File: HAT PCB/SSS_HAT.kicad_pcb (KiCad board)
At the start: 2 copper layers, 24 parts, among them J1 Conn_01x22_Socket, J2 Conn_01x22_Socket, J3 CAN0, J4 CAN1, J5 I2C0, J6 I2C1, SW1 CAN0_Pulldown, SW2 CAN1_Pulldown, SW3 I2C0_Pulldown, SW4 I2C1_Pulldown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

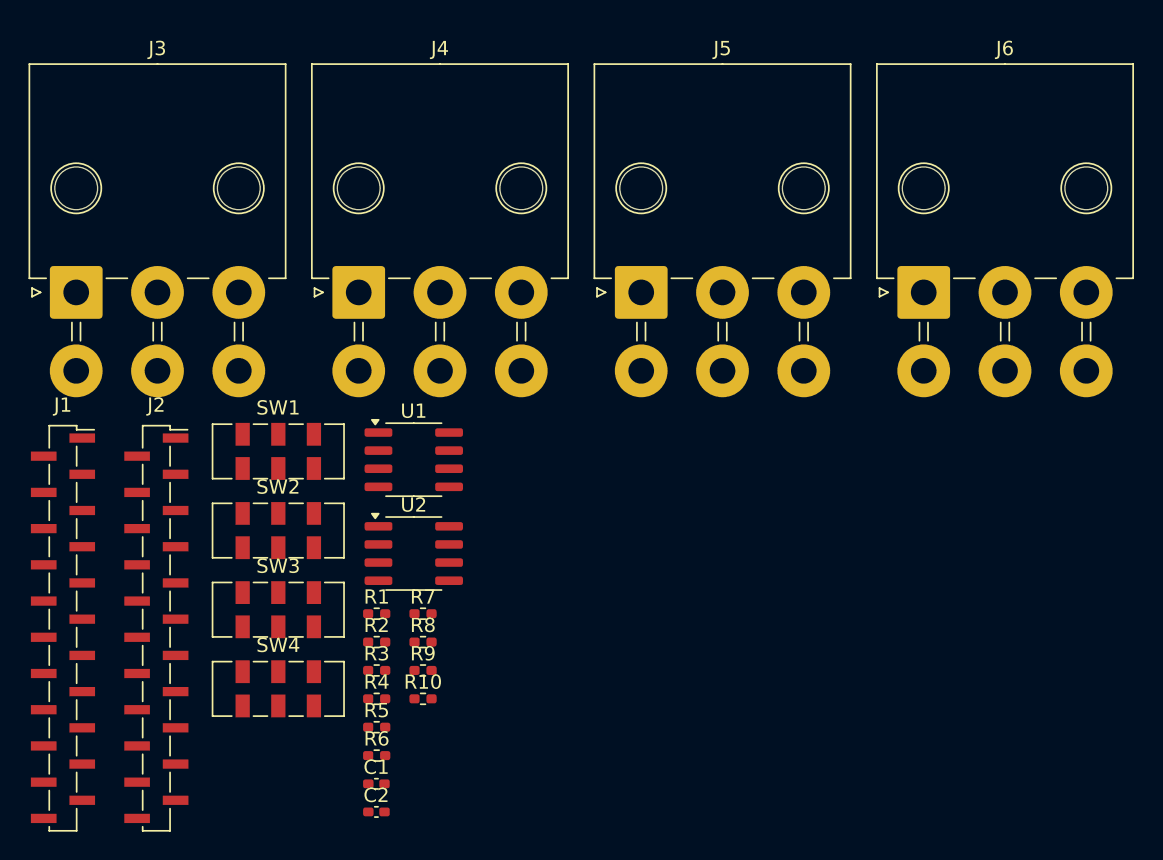
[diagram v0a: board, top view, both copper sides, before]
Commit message: Added 2 Channel 18-bit ADC
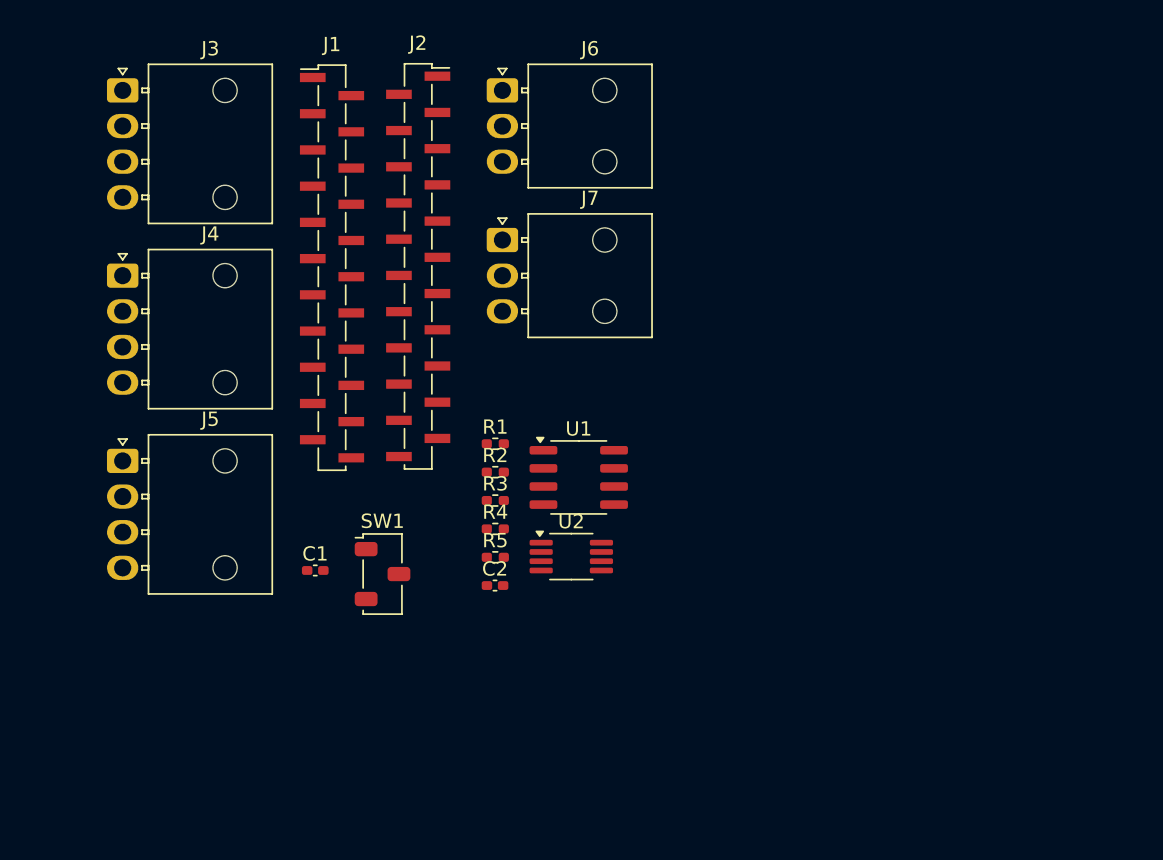
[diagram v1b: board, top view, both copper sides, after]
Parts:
- removed R10, R7, R8, R9: 2k2, Resistor_SMD:R_0402_1005Metric_Pad0.72x0.64mm_HandSolder
- removed R6: 60, Resistor_SMD:R_0402_1005Metric_Pad0.72x0.64mm_HandSolder
- removed SW2: CAN1_Pulldown, Button_Switch_SMD:SW_DPDT_CK_JS202011JCQN
- removed SW3: I2C0_Pulldown, Button_Switch_SMD:SW_DPDT_CK_JS202011JCQN
- removed SW4: I2C1_Pulldown, Button_Switch_SMD:SW_DPDT_CK_JS202011JCQN
- added J7: ADC_1, Connector_Molex:Molex_Nano-Fit_105313-xx03_1x03_P2.50mm_Horizontal, F.Cu at (152.1, 58.3)
- C1: value 4.7nF -> 0.1μF
- C2: value 4.7nF -> 10μF
- J1: value Conn_01x22_Socket -> ESP32_Connector_0; footprint Connector_PinSocket_1.27mm:PinSocket_1x22_P1.27mm_Vertical_SMD_Pin1Right -> Connector_PinSocket_1.27mm:PinSocket_1x22_P1.27mm_Vertical_SMD_Pin1Left
- J2: value Conn_01x22_Socket -> ESP32_Connector_1
- J3: value CAN0 -> CAN; footprint Connector_Molex:Molex_Mega-Fit_76825-0006_2x03_P5.70mm_Horizontal -> Connector_Molex:Molex_Nano-Fit_105313-xx04_1x04_P2.50mm_Horizontal
- J4: value CAN1 -> CAN; footprint Connector_Molex:Molex_Mega-Fit_76825-0006_2x03_P5.70mm_Horizontal -> Connector_Molex:Molex_Nano-Fit_105313-xx04_1x04_P2.50mm_Horizontal
- J5: value I2C0 -> I2C; footprint Connector_Molex:Molex_Mega-Fit_76825-0006_2x03_P5.70mm_Horizontal -> Connector_Molex:Molex_Nano-Fit_105313-xx04_1x04_P2.50mm_Horizontal
- J6: value I2C1 -> ADC_0; footprint Connector_Molex:Molex_Mega-Fit_76825-0006_2x03_P5.70mm_Horizontal -> Connector_Molex:Molex_Nano-Fit_105313-xx03_1x03_P2.50mm_Horizontal
- R2, R3, R5: value 60 -> 2k2
- R4: value 120 -> 2k2
- SW1: value CAN0_Pulldown -> I2C; footprint Button_Switch_SMD:SW_DPDT_CK_JS202011JCQN -> Button_Switch_SMD:Nidec_Copal_CAS-120A
- U2: value TJA1051T -> MCP3422Axx-xMS; footprint Package_SO:SOIC-8_3.9x4.9mm_P1.27mm -> Package_SO:MSOP-8_3x3mm_P0.65mm
- moved J5 38.2 mm to (125.4, 73.8)
- moved J6 32.8 mm to (152.1, 47.8)
- moved J1 31.5 mm to (140.1, 60.3)
- moved J2 31.3 mm to (146.2, 60.2)
- moved C2 17.9 mm to (151.5, 82.6)
- moved J4 16.6 mm to (125.4, 60.8)
- moved C1 15.6 mm to (138.9, 81.5)
- moved J3 14.5 mm to (125.4, 47.8)
- moved R1 14.5 mm to (151.6, 72.6)
- moved R3 14.5 mm to (151.6, 76.6)
- moved R4 14.5 mm to (151.6, 78.6)
- moved R2 14.5 mm to (151.6, 74.6)
- moved R5 14.5 mm to (151.6, 80.6)
- moved U1 11.6 mm to (157.4, 75.0)
- moved SW1 11.3 mm to (143.7, 81.8)
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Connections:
- net CAN0_RX renamed CAN_RX
- net CAN0_TX renamed CAN_TX
- C1 pad 1: Net-(C1-Pad1) -> +3.3V
- C2 pad 1: Net-(C2-Pad1) -> +3.3V
- J1 pad 12: ADC1_7 -> unconnected-(J1-Pin_12-Pad12)
- J1 pad 13: ADC1_2 -> unconnected-(J1-Pin_13-Pad13)
- J1 pad 19: CAN0_S -> unconnected-(J1-Pin_19-Pad19)
- J1 pad 20: CAN1_S -> unconnected-(J1-Pin_20-Pad20)
- J1 pad 6: ADC1_5 -> unconnected-(J1-Pin_6-Pad6)
- J1 pad 7: ADC1_6 -> unconnected-(J1-Pin_7-Pad7)
- J1 pad 8: CAN1_TX -> CAN_S
- J1 pad 9: CAN1_RX -> unconnected-(J1-Pin_9-Pad9)
- J2 pad 4: ADC1_0 -> unconnected-(J2-Pin_4-Pad4)
- J2 pad 5: ADC1_1 -> unconnected-(J2-Pin_5-Pad5)
- J2 pad 6: I2C0_SDA -> I2C_SDA
- J2 pad 7: I2C0_SCL -> I2C_SCL
- J2 pad 8: I2C1_SDA -> ADC_SDA
- J2 pad 9: I2C1_SCL -> ADC_SCL
- J3 pad 1: Net-(J3-Pin_1) -> +5V
- J3 pad 2: unconnected-(J3-Pin_2-Pad2) -> GND
- J3 pad 3: Net-(J3-Pin_3) -> CANH
- J3 pad 4: +5V -> CANL
- J4 pad 1: Net-(J4-Pin_1) -> +5V
- J4 pad 2: unconnected-(J4-Pin_2-Pad2) -> GND
- J4 pad 3: Net-(J4-Pin_3) -> CANH
- J4 pad 4: +5V -> CANL
- J5 pad 1: I2C0_SCL -> +5V
- J5 pad 2: unconnected-(J5-Pin_2-Pad2) -> GND
- J5 pad 3: I2C0_SDA -> I2C_SCL
- J5 pad 4: +5V -> I2C_SDA
- J6 pad 1: I2C1_SCL -> +5V
- J6 pad 2: unconnected-(J6-Pin_2-Pad2) -> GND
- J6 pad 3: I2C1_SDA -> ADC_0
- R1 pad 1: Net-(J3-Pin_3) -> CANL
- R1 pad 2: Net-(J3-Pin_1) -> CANH
- R2 pad 1: Net-(SW1A-A) -> Net-(SW1-C)
- R2 pad 2: Net-(C1-Pad1) -> I2C_SCL
- R3 pad 1: Net-(SW1B-A) -> Net-(SW1-C)
- R3 pad 2: Net-(C1-Pad1) -> I2C_SDA
- R4 pad 1: Net-(J4-Pin_3) -> +3.3V
- R4 pad 2: Net-(J4-Pin_1) -> ADC_SCL
- R5 pad 1: Net-(SW2A-A) -> +3.3V
- R5 pad 2: Net-(C2-Pad1) -> ADC_SDA
- SW1 pad 1: Net-(SW1A-A) -> Net-(SW1-C)
- SW1 pad 2: Net-(J3-Pin_1) -> +3.3V
- U1 pad 6: Net-(J3-Pin_3) -> CANL
- U1 pad 7: Net-(J3-Pin_1) -> CANH
- U1 pad 8: CAN0_S -> CAN_S
- U2 pad 1: CAN1_TX -> ADC_0
- U2 pad 3: +5V -> +3.3V
- U2 pad 4: CAN1_RX -> ADC_SDA
- U2 pad 5: unconnected-(U2-NC-Pad5) -> ADC_SCL
- U2 pad 6: Net-(J4-Pin_3) -> GND
- U2 pad 7: Net-(J4-Pin_1) -> ADC_2
- U2 pad 8: CAN1_S -> GND
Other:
- copper layers 2 -> 4

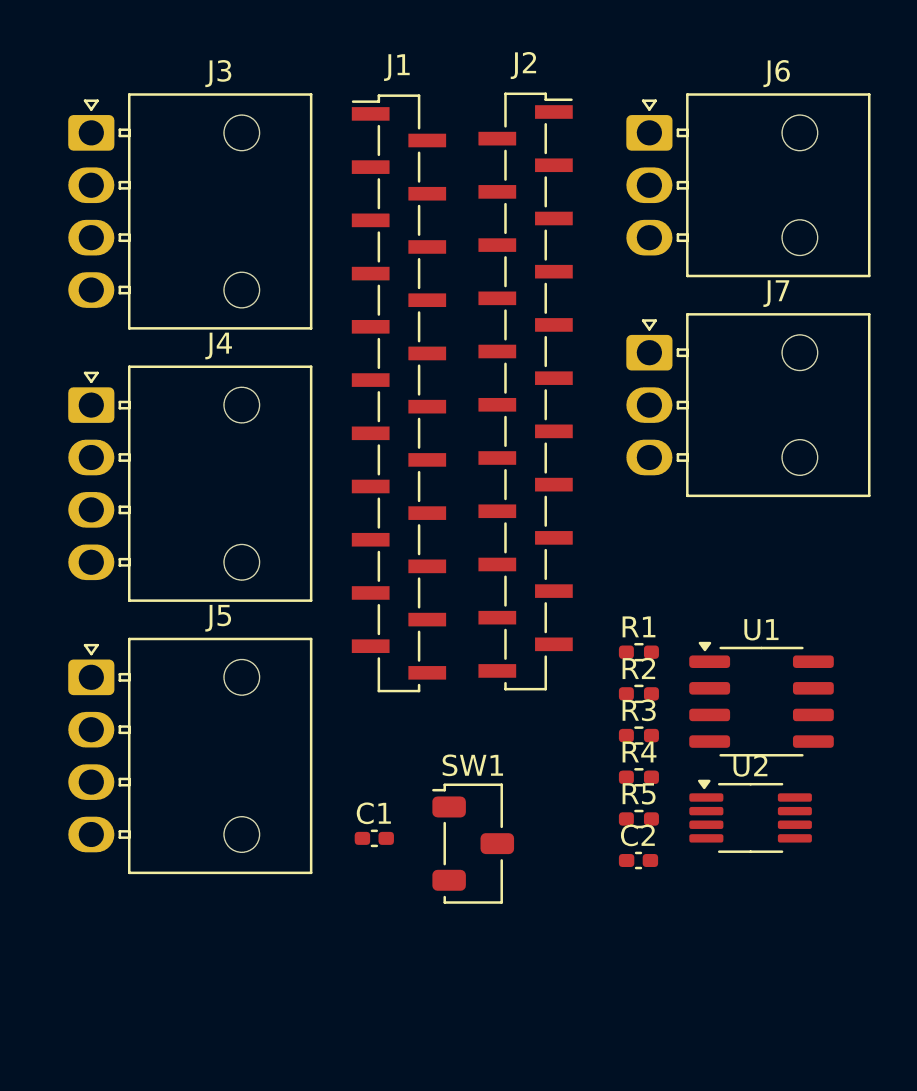
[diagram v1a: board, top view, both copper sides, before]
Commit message: added IMU
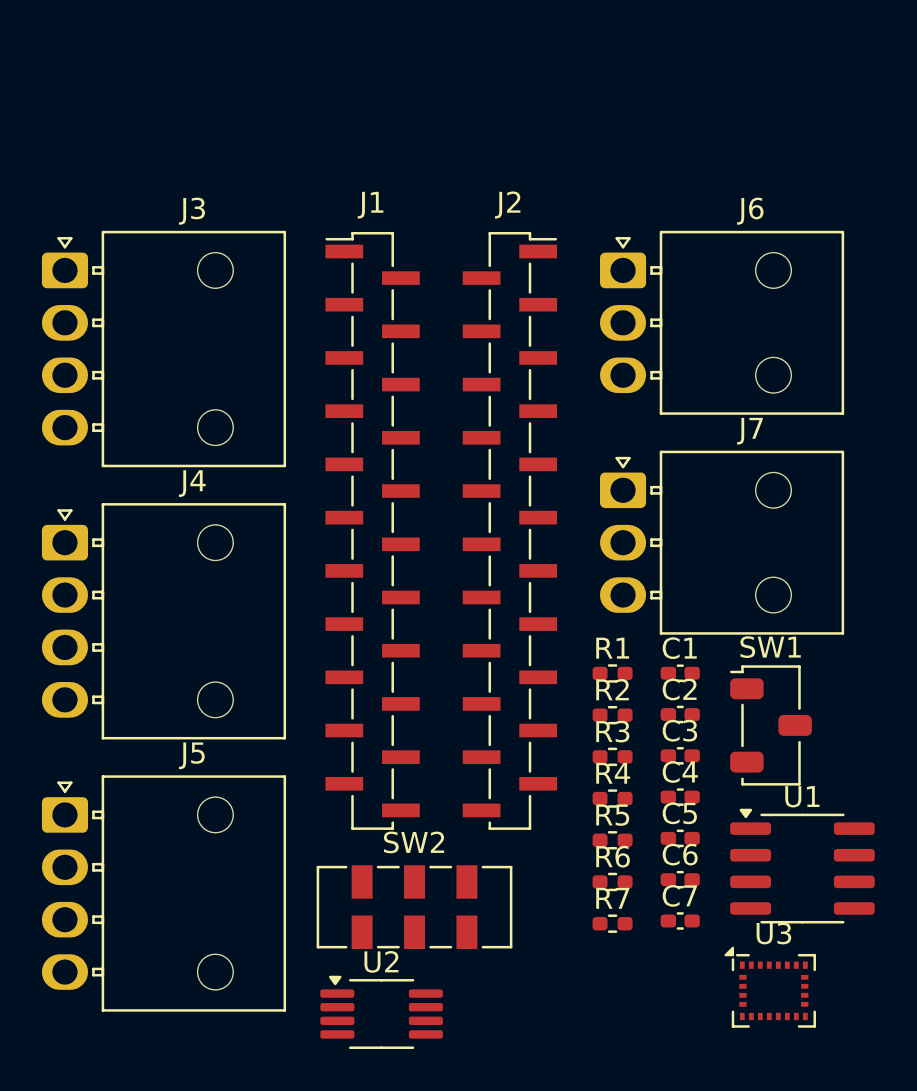
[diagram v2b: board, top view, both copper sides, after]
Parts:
- added C3: 0.1μF, Capacitor_SMD:C_0402_1005Metric_Pad0.74x0.62mm_HandSolder, F.Cu at (153.5, 77.6)
- added C4: 10μF, Capacitor_SMD:C_0402_1005Metric_Pad0.74x0.62mm_HandSolder, F.Cu at (153.5, 79.5)
- added C5: 0.1μF, Capacitor_SMD:C_0402_1005Metric_Pad0.74x0.62mm_HandSolder, F.Cu at (153.5, 81.5)
- added C6: 10nF, Capacitor_SMD:C_0402_1005Metric_Pad0.74x0.62mm_HandSolder, F.Cu at (153.5, 83.5)
- added C7: 0.1μF, Capacitor_SMD:C_0402_1005Metric_Pad0.74x0.62mm_HandSolder, F.Cu at (153.5, 85.4)
- added R6: 10k, Resistor_SMD:R_0402_1005Metric_Pad0.72x0.64mm_HandSolder, F.Cu at (150.3, 83.6)
- added R7: 10k, Resistor_SMD:R_0402_1005Metric_Pad0.72x0.64mm_HandSolder, F.Cu at (150.3, 85.6)
- added SW2: IMU_SPI_Pullup, Button_Switch_SMD:SW_DPDT_CK_JS202011JCQN, F.Cu at (140.8, 84.8)
- added U3: LSM9DS1, Package_LGA:LGA-24L_3x3.5mm_P0.43mm, F.Cu at (158.0, 88.8)
- R2, R3: value 2k2 -> 10k
- moved U2 19.9 mm to (139.3, 89.9)
- moved C1 16.6 mm to (153.5, 73.6)
- moved SW1 15.3 mm to (157.9, 76.1)
- moved U1 8.20 mm to (159.4, 82.9)
- moved C2 7.24 mm to (153.5, 75.6)
- moved J2 6.70 mm to (145.4, 66.8)
- moved J1 6.68 mm to (138.8, 66.8)
- moved J3 6.68 mm to (124.2, 54.4)
- moved J4 6.68 mm to (124.2, 67.4)
- moved J5 6.68 mm to (124.2, 80.4)
- moved J6 6.68 mm to (150.8, 54.4)
- moved J7 6.68 mm to (150.8, 64.9)
- moved R1 1.62 mm to (150.3, 73.6)
- moved R2 1.62 mm to (150.3, 75.6)
- moved R3 1.62 mm to (150.3, 77.6)
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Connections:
- J1 pad 10: unconnected-(J1-Pin_10-Pad10) -> IMU_SDA
- J1 pad 11: unconnected-(J1-Pin_11-Pad11) -> IMU_SCL

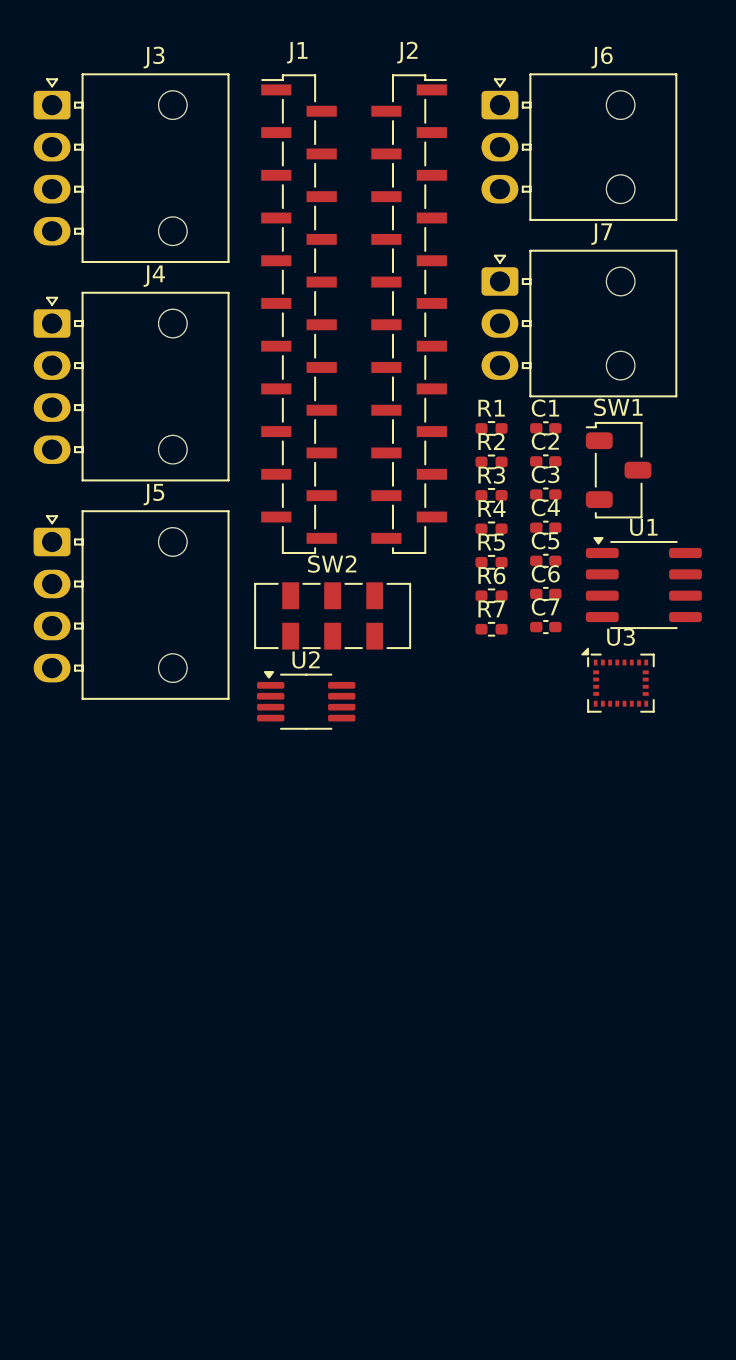
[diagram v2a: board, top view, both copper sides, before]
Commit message: Routed PCB & Replaced IMU for ICM-42688-P
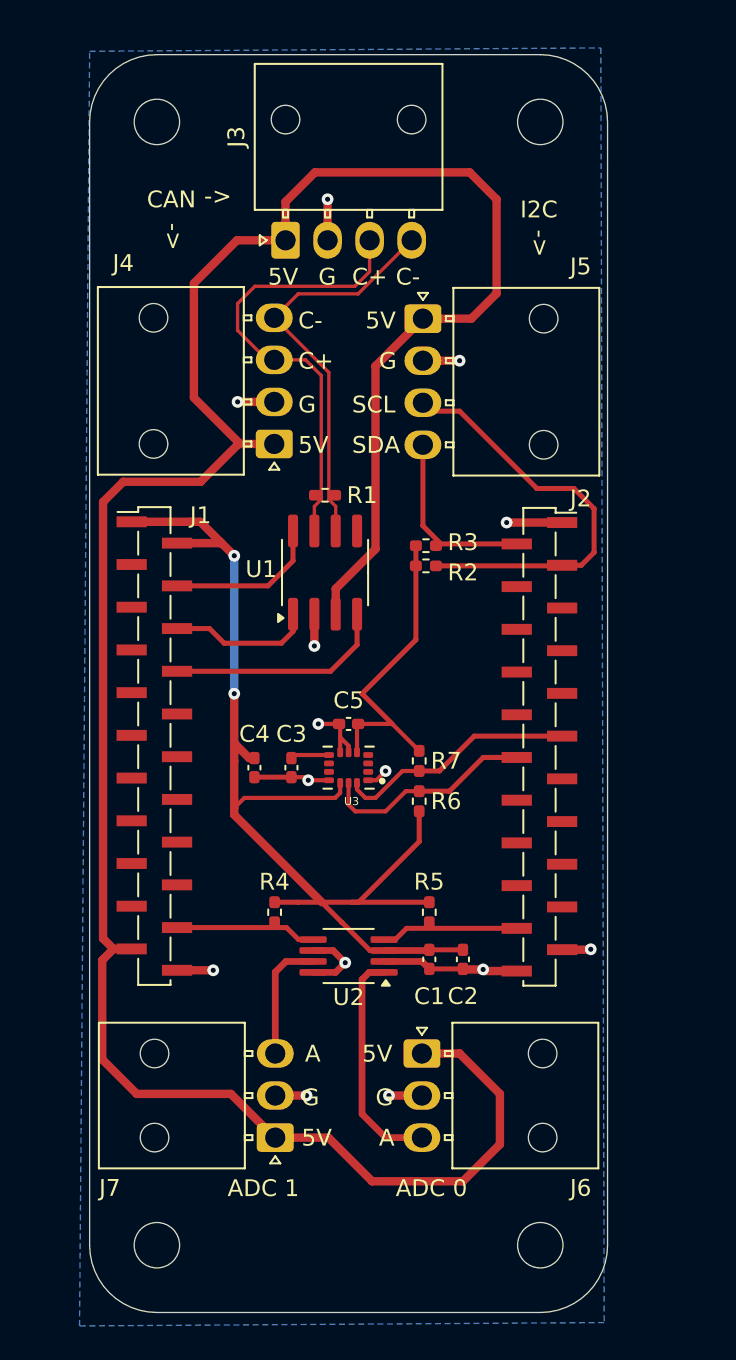
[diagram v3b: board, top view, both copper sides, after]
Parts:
- removed C6: 10nF, Capacitor_SMD:C_0402_1005Metric_Pad0.74x0.62mm_HandSolder
- removed C7: 0.1μF, Capacitor_SMD:C_0402_1005Metric_Pad0.74x0.62mm_HandSolder
- removed SW1: I2C, Button_Switch_SMD:Nidec_Copal_CAS-120A
- removed SW2: IMU_SPI_Pullup, Button_Switch_SMD:SW_DPDT_CK_JS202011JCQN
- added H1: MountingHole, MountingHole:MountingHole_2.7mm_M2.5, F.Cu at (130.4, 55.4)
- added H2: MountingHole, MountingHole:MountingHole_2.7mm_M2.5, F.Cu at (153.2, 55.4)
- added H3: MountingHole, MountingHole:MountingHole_2.7mm_M2.5, F.Cu at (153.2, 122.2)
- added H4: MountingHole, MountingHole:MountingHole_2.7mm_M2.5, F.Cu at (130.4, 122.2)
- C4: value 10μF -> 2.2μF
- U3: value LSM9DS1 -> ICM-42688-P; footprint Package_LGA:LGA-24L_3x3.5mm_P0.43mm -> ICM-42688-P:PQFN50P300X250X97-14N
- moved J6 56.6 mm to (146.2, 110.8)
- moved J7 52.6 mm to (137.4, 115.8), turned to 180 degrees
- moved C1 32.3 mm to (146.6, 105.2), turned to -90 degrees
- moved C2 30.0 mm to (148.6, 105.2), turned to -90 degrees
- moved J1 27.1 mm to (130.2, 92.5)
- moved J2 26.9 mm to (153.2, 92.6)
- moved R4 26.2 mm to (137.4, 102.4), turned to -90 degrees
- moved J5 25.7 mm to (146.2, 67.1)
- moved C4 22.4 mm to (136.2, 93.8), turned to 90 degrees
- moved C3 22.2 mm to (138.4, 93.8), turned to 90 degrees
- moved R5 21.1 mm to (146.6, 102.4), turned to -90 degrees
- moved U1 19.0 mm to (140.4, 82.2), turned to 90 degrees
- moved U3 17.0 mm to (141.8, 93.8), turned to 180 degrees
- moved J3 16.0 mm to (138.1, 62.4), turned to 90 degrees
- moved U2 15.3 mm to (141.8, 105.0), turned to 180 degrees
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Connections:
- net CANH renamed CAN+
- net CANL renamed CAN-
- C5 pad 1: GND -> +3.3V
- C5 pad 2: +3.3V -> GND
- J1 pad 10: IMU_SDA -> unconnected-(J1-Pin_10-Pad10)
- J1 pad 11: IMU_SCL -> unconnected-(J1-Pin_11-Pad11)
- J1 pad 20: unconnected-(J1-Pin_20-Pad20) -> ADC_SCL
- J1 pad 4: CAN_TX -> CAN_S
- J1 pad 5: CAN_RX -> unconnected-(J1-Pin_5-Pad5)
- J1 pad 6: unconnected-(J1-Pin_6-Pad6) -> CAN_TX
- J1 pad 8: CAN_S -> CAN_RX
- J2 pad 11: unconnected-(J2-Pin_11-Pad11) -> IMU_SDA
- J2 pad 12: unconnected-(J2-Pin_12-Pad12) -> IMU_SCL
- J2 pad 2: unconnected-(J2-Pin_2-Pad2) -> I2C_SDA
- J2 pad 20: unconnected-(J2-Pin_20-Pad20) -> ADC_SDA
- J2 pad 3: unconnected-(J2-Pin_3-Pad3) -> I2C_SCL
- J2 pad 6: I2C_SDA -> unconnected-(J2-Pin_6-Pad6)
- J2 pad 7: I2C_SCL -> unconnected-(J2-Pin_7-Pad7)
- J2 pad 8: ADC_SDA -> unconnected-(J2-Pin_8-Pad8)
- J2 pad 9: ADC_SCL -> unconnected-(J2-Pin_9-Pad9)
- R2 pad 1: Net-(SW1-C) -> +3.3V
- R3 pad 1: Net-(SW1-C) -> +3.3V
- R6 pad 2: Net-(SW2A-C) -> +3.3V
- R7 pad 2: Net-(SW2B-C) -> +3.3V
- U2 pad 7: ADC_2 -> ADC_1
- U3 pad 1: +3.3V -> GND
- U3 pad 11: unconnected-(U3-INT1_A/G-Pad11) -> GND
- U3 pad 12: unconnected-(U3-INT2_A/G-Pad12) -> +3.3V
- U3 pad 13: unconnected-(U3-DEN_A/G-Pad13) -> IMU_SCL
- U3 pad 14: GND -> IMU_SDA
- U3 pad 2: IMU_SCL -> unconnected-(U3-RESV_2-Pad2)
- U3 pad 3: +3.3V -> unconnected-(U3-RESV_3-Pad3)
- U3 pad 4: IMU_SDA -> unconnected-(U3-INT1/INT-Pad4)
- U3 pad 5: GND -> +3.3V
- U3 pad 7: unconnected-(U3-CS_A/G-Pad7) -> GND
- U3 pad 8: unconnected-(U3-CS_M-Pad8) -> +3.3V
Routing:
- net +5V: track 0.00 -> 146.3 mm
- net +3.3V: track 0.00 -> 88.3 mm, vias 0 -> 2
- net GND: track 0.00 -> 42.3 mm, vias 0 -> 14
- net CAN+: track 0.00 -> 27.6 mm
- net I2C_SCL: track 0.00 -> 25.9 mm
- net CAN-: track 0.00 -> 24.3 mm
- net IMU_SDA: track 0.00 -> 14.4 mm
- net ADC_0: track 0.00 -> 13.6 mm
- net CAN_RX: track 0.00 -> 13.2 mm
- net IMU_SCL: track 0.00 -> 12.8 mm
- net I2C_SDA: track 0.00 -> 11.7 mm
- net CAN_S: track 0.00 -> 9.29 mm
- net CAN_TX: track 0.00 -> 8.57 mm
- net ADC_SCL: track 0.00 -> 8.38 mm
- net ADC_SDA: track 0.00 -> 8.17 mm
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- added copper zone on B.Cu, net GND
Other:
- board outline added: 30.8 x 74.8 mm
- copper layers 4 -> 2
- board text added: "->"
- board text added: "5V"
- board text added: "A"
- board text added: "ADC 0"
- board text added: "ADC 1"
- board text added: "C+"
- board text added: "C-"
- board text added: "CAN"
- board text added: "G"
- board text added: "I2C"
- board text added: "SCL"
- board text added: "SDA"
